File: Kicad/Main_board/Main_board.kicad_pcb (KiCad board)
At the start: 2 copper layers, 100 x 100 mm, 28 parts, among them J1 LIPO 2S, J10 DIST_FRONT, J11 SENSORES_LINEA, J12 DIST_DCHA, J2 MOT_IZQ, J3 TB6612FNG_A, J4 TB6612FNG_B, J5 DC-DC_5V, J6 HC-05, J7 MOT_DER, J8 DIST_IZQ, J9 CAMARA, SW1 SW_DPDT, SW2 SW_Push, SW3 SW_Push, U1 PCF8574

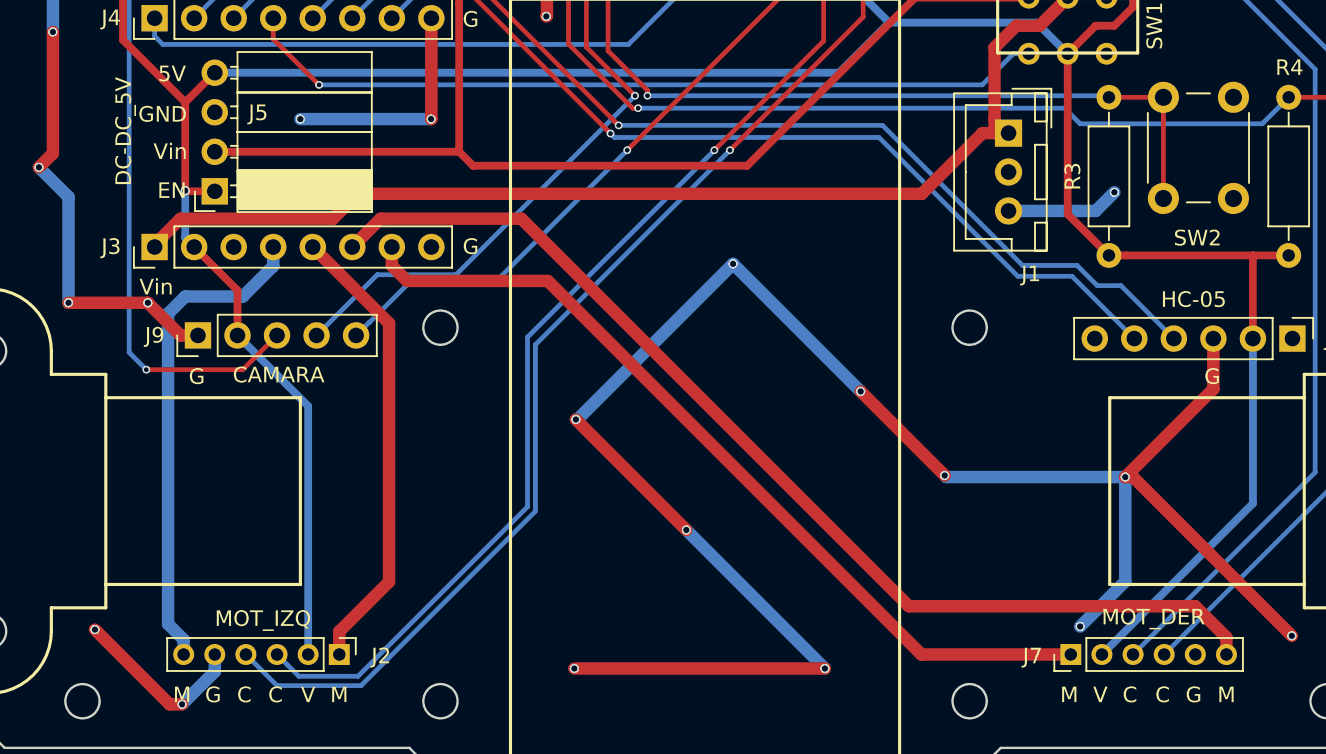
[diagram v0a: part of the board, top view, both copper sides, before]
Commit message: Motor driver position adjusted
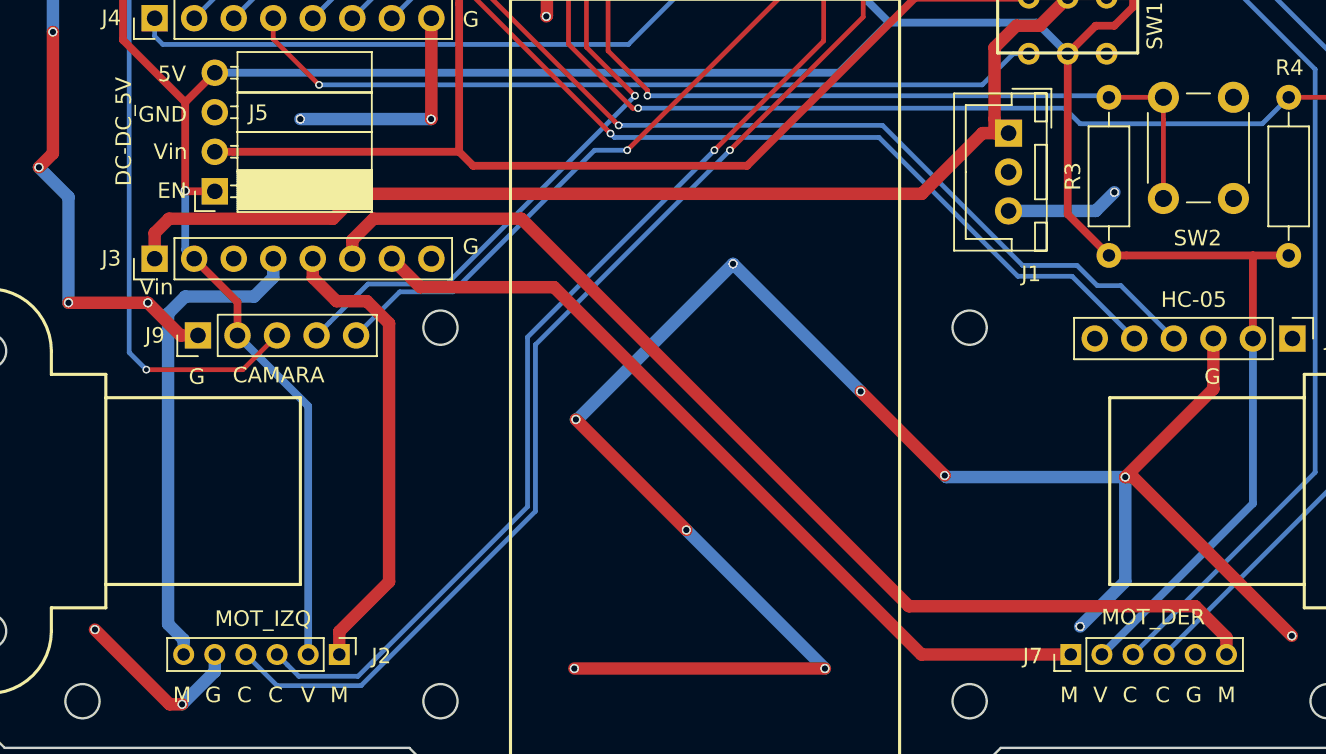
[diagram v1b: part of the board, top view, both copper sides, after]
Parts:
- moved J3 0.75 mm to (114.6, 114.6)
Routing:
- net +BATT: track 69.5 -> 70.7 mm
- net M_DER_+: track 55.2 -> 54.2 mm
- net M_DER_-: track 69.2 -> 70.2 mm

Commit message: BOMs and PDF schematic added
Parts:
- D3: value 1N4003 -> 1N4001
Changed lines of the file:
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@@
     (links 90)
     (no_connects 0)
-    (area 99.899999 44.8 200.100001 150.100001)
+    (area 99.924999 49.924999 200.075001 150.075001)
     (thickness 1.6)
     (drawings 108)
@@
       (effects (font (size 1 1) (thickness 0.15)))
     )
-    (fp_text value 1N4003 (at 5.08 2.41 180) (layer F.Fab)
-      (effects (font (size 1 1) (thickness 0.15)))
-    )
+    (fp_text value 1N4001 (at 5.08 2.41 180) (layer F.Fab)
+      (effects (font (size 1 1) (thickness 0.15)))
+    )
